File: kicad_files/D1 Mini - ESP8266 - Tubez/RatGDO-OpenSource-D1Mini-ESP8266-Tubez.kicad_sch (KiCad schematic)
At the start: 23 parts, among them J1 Screw_Terminal_01x03, J2 Conn_01x11, J3 Screw_Terminal_01x02, Q1 2N7002, Q2 AO3400A, Q3 AO3400A, Q4 AO3400A, U1 WeMos_D1_mini, U2 K7805-500R3

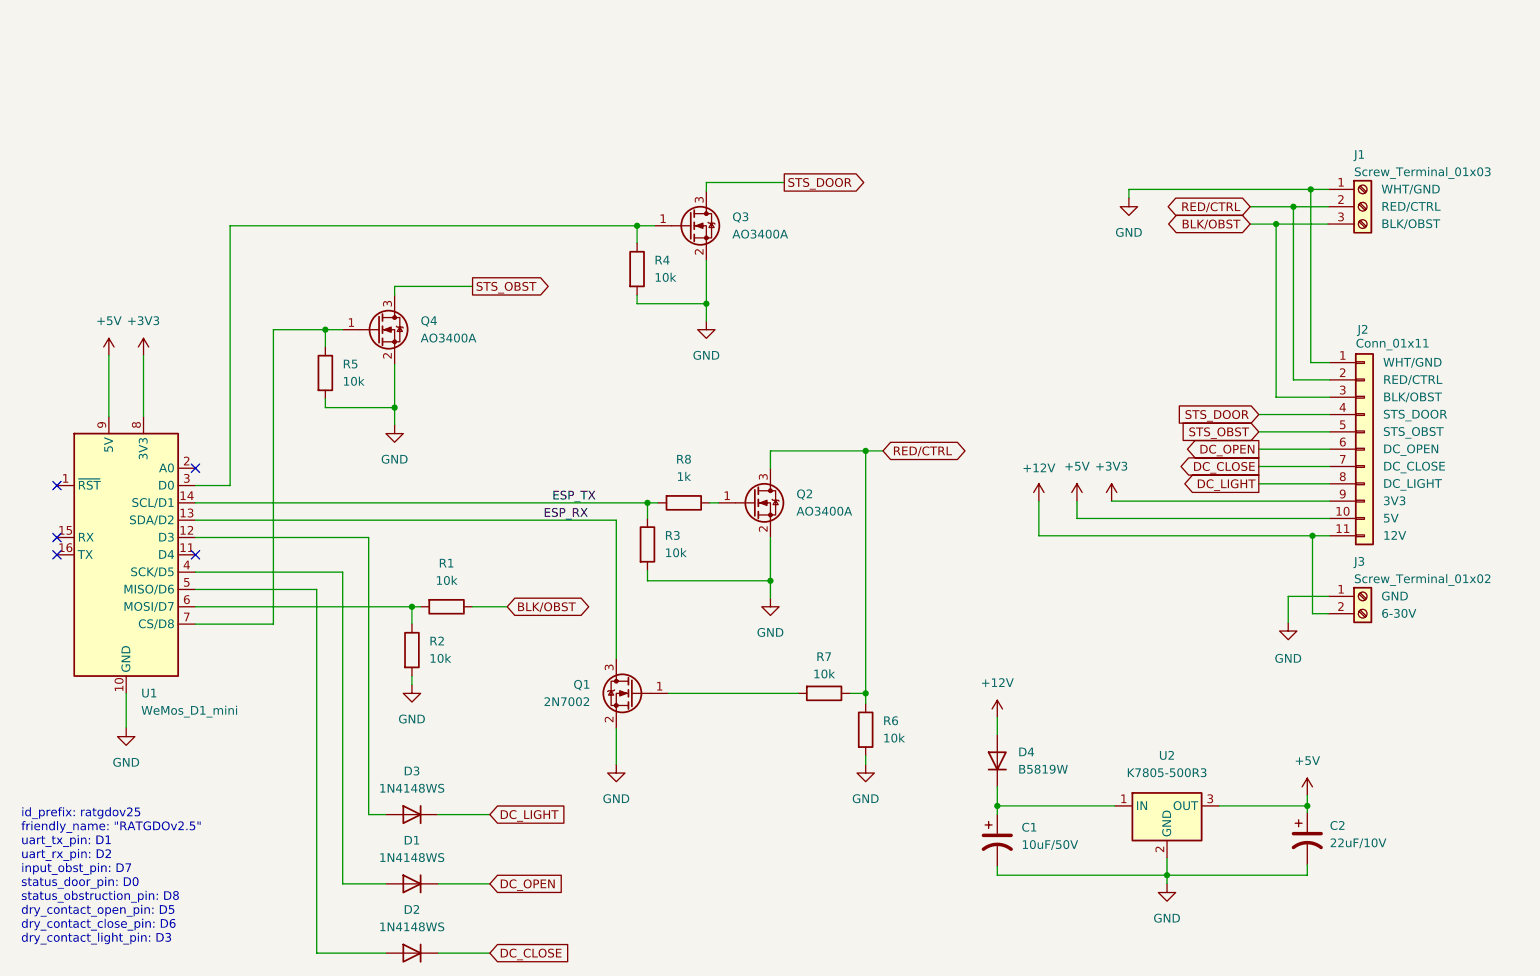
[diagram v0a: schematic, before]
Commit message: addition of LEDs
work in progress
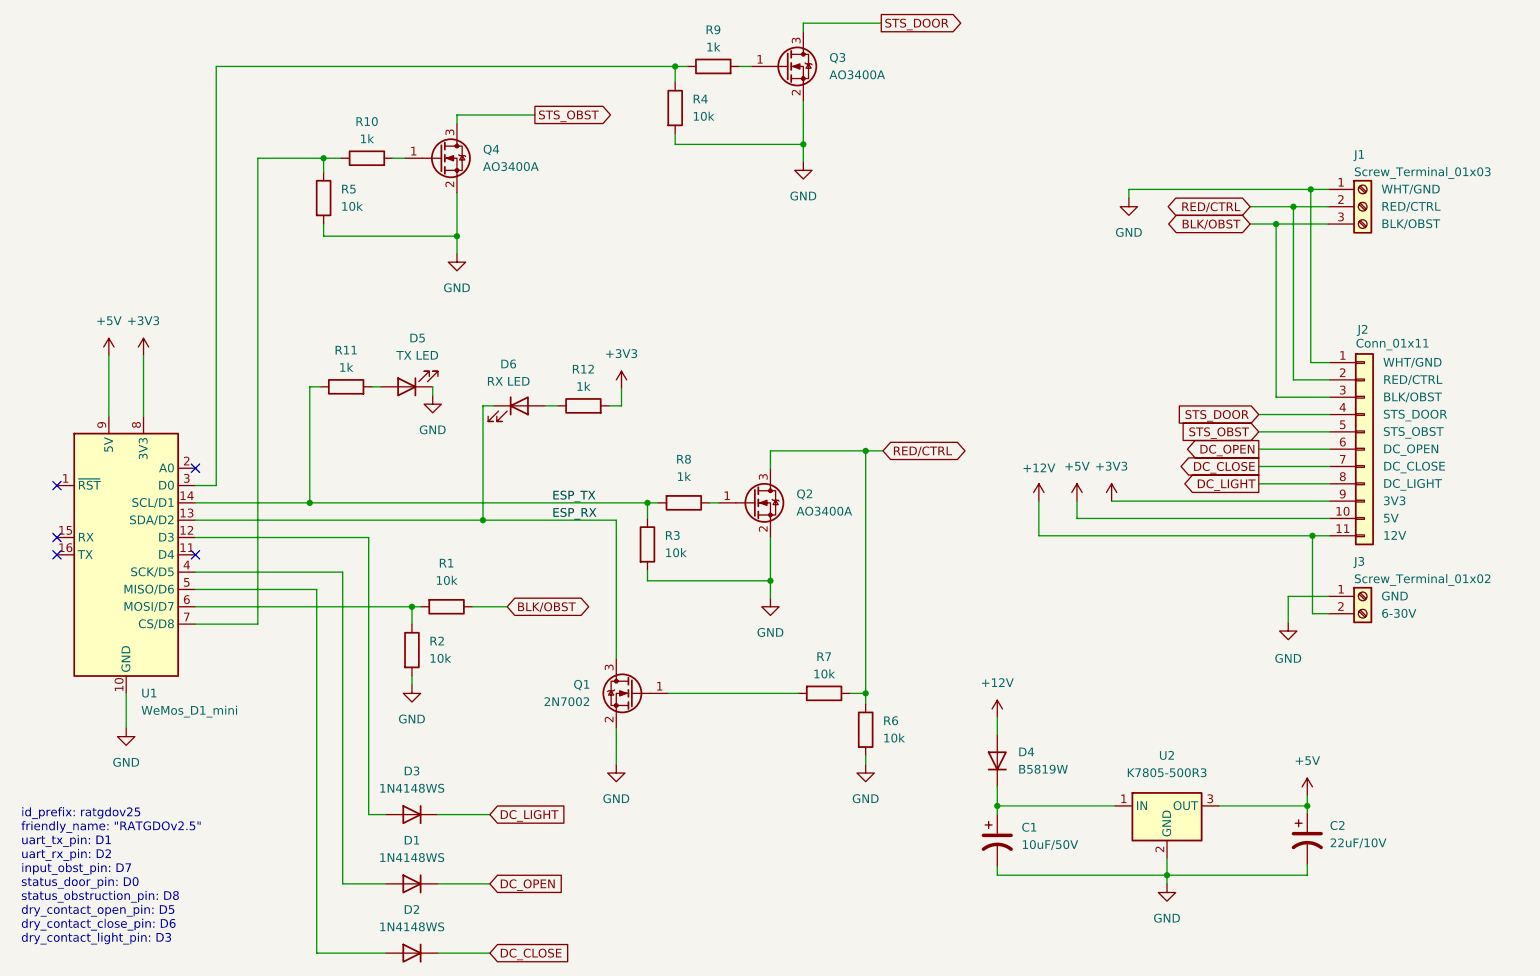
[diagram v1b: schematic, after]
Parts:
- added D5: TX LED, LED_SMD:LED_0805_2012Metric_Pad1.15x1.40mm_HandSolder, symbol Device:LED
- added D6: RX LED, LED_SMD:LED_0805_2012Metric_Pad1.15x1.40mm_HandSolder, symbol Device:LED
- added R10, R11, R12, R9: 1k, Resistor_SMD:R_0805_2012Metric_Pad1.20x1.40mm_HandSolder, symbol Device:R
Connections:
- net +3V3: now also R12.2
- net ESP_RX: now also D6.1 (K)
- net ESP_TX: now also R11.1
- net GND: now also D5.1 (K)
- net at R5.1, U1.7 (CS/D8): now also R10.1; no longer Q4.1 (G)
- net at R4.1, U1.3 (D0): now also R9.1; no longer Q3.1 (G)
- new net: D5.2 (A), R11.2
- new net: D6.2 (A), R12.1
- new net: Q3.1 (G), R9.2
- new net: Q4.1 (G), R10.2
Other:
- moved on the sheet: Q3, Q4, R4, R5

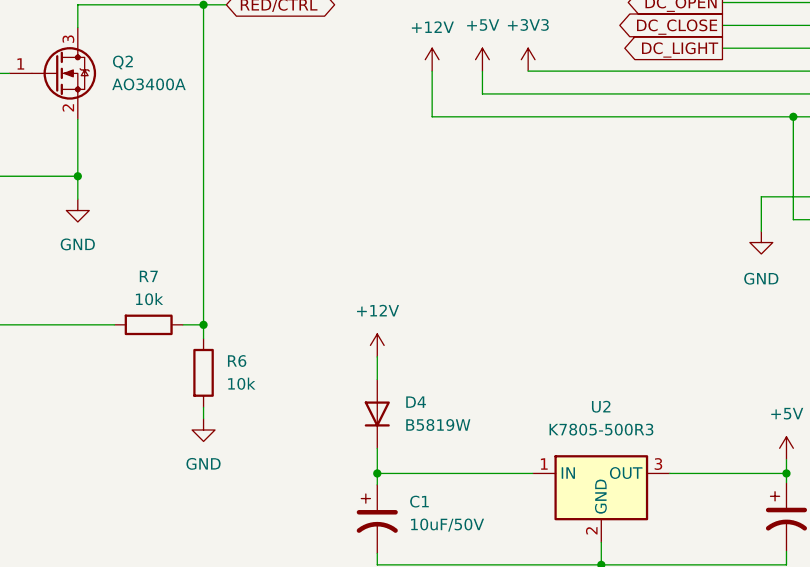
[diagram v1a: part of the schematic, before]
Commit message: Add 750mA fuse
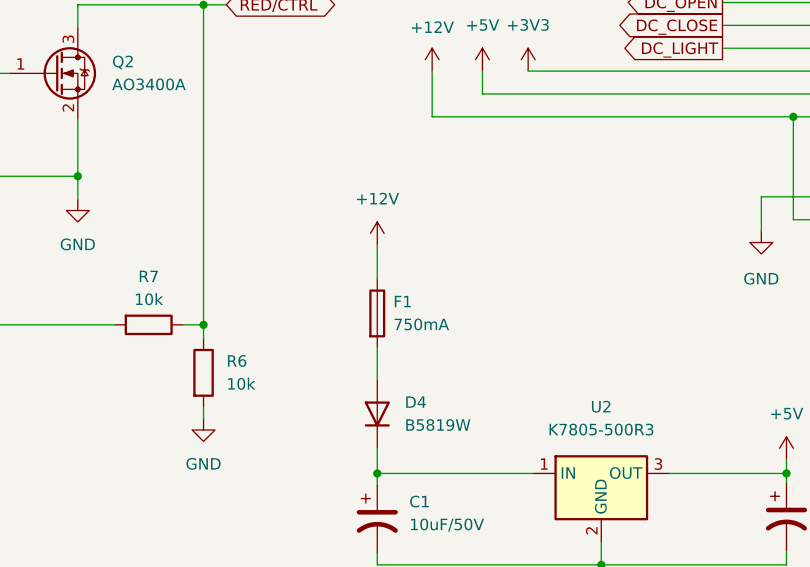
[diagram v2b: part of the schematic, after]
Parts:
- added F1: 750mA, Fuse:Fuse_1206_3216Metric_Pad1.42x1.75mm_HandSolder, symbol Device:Fuse
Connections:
- net +12V: now also F1.1; no longer D4.2 (A)
- new net: D4.2 (A), F1.2
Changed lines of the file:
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@@
     (stroke (width 0) (type default))
   )
-  (wire (pts (xy 172.212 125.476) (xy 172.212 128.016))
+  (wire (pts (xy 172.212 124.46) (xy 172.212 128.016))
+    (stroke (width 0) (type default))
+  )
+  (wire (pts (xy 172.212 113.03) (xy 172.212 116.84))
     (stroke (width 0) (type default))
   )
@@
     )
   )
-  (symbol (lib_id "power:+12V") (at 172.212 125.476 0) (unit 1)
-    (in_bom yes) (on_board yes) (dnp no) (fields_autoplaced)
-    (property "Reference" "#PWR013" (at 172.212 129.286 0)
-      (effects (font (size 1.27 1.27)) hide)
-    )
-    (property "Value" "+12V" (at 172.212 120.396 0)
-      (effects (font (size 1.27 1.27)))
-    )
-    (property "Footprint" "" (at 172.212 125.476 0)
-      (effects (font (size 1.27 1.27)) hide)
-    )
-    (property "Datasheet" "" (at 172.212 125.476 0)
-      (effects (font (size 1.27 1.27)) hide)
-    )
+  (symbol (lib_id "Device:Fuse") (at 172.212 120.65 0) (unit 1)
+    (in_bom yes) (on_board yes) (dnp no) (fields_autoplaced)
+    (property "Reference" "F1" (at 173.99 119.38 0)
+      (effects (font (size 1.27 1.27)) (justify left))
+    )
+    (property "Value" "750mA" (at 173.99 121.92 0)
+      (effects (font (size 1.27 1.27)) (justify left))
+    )
+    (property "Footprint" "Fuse:Fuse_1206_3216Metric_Pad1.42x1.75mm_HandSolder" (at 170.434 120.65 90)
+      (effects (font (size 1.27 1.27)) hide)
+    )
+    (property "Datasheet" "~" (at 172.212 120.65 0)
+      (effects (font (size 1.27 1.27)) hide)
+    )
+    (pin "2")
+    (pin "1")
+    (instances
+      (project "RatGDO-OpenSource-D1Mini-ESP8266-Tubez"
+        (path "/d526daf5-1a87-4c4a-b8db-6120ccadc008"
+          (reference "F1") (unit 1)
+        )
+      )
+    )
+  )
+  (symbol (lib_id "power:+12V") (at 172.212 113.03 0) (unit 1)
+    (in_bom yes) (on_board yes) (dnp no) (fields_autoplaced)
+    (property "Reference" "#PWR013" (at 172.212 116.84 0)
+      (effects (font (size 1.27 1.27)) hide)
+    )
+    (property "Value" "+12V" (at 172.212 107.95 0)
+      (effects (font (size 1.27 1.27)))
+    )
+    (property "Footprint" "" (at 172.212 113.03 0)
+      (effects (font (size 1.27 1.27)) hide)
+    )
+    (property "Datasheet" "" (at 172.212 113.03 0)
+      (effects (font (size 1.27 1.27)) hide)
+    )
